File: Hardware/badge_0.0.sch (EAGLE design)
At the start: 43 parts, among them CON1 PH_2, IC1 CP2102, SW1 MK12C02, SW2 MK12C02, U4 MCP73832T-2DCI/OT

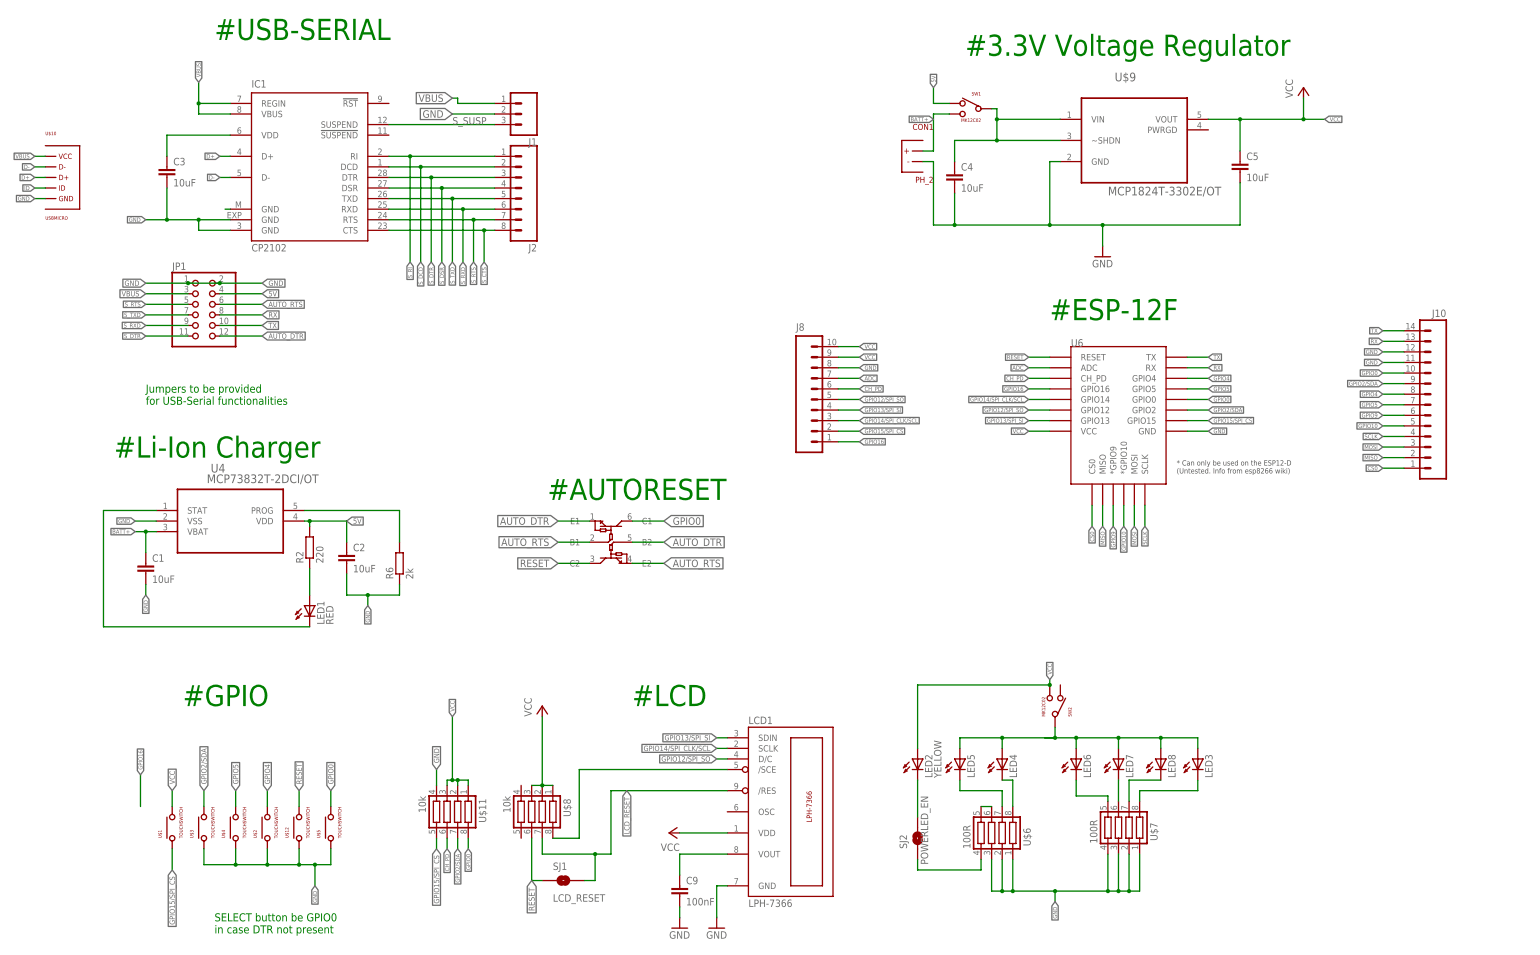
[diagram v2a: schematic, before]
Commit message: Rerouted and labeled some nets
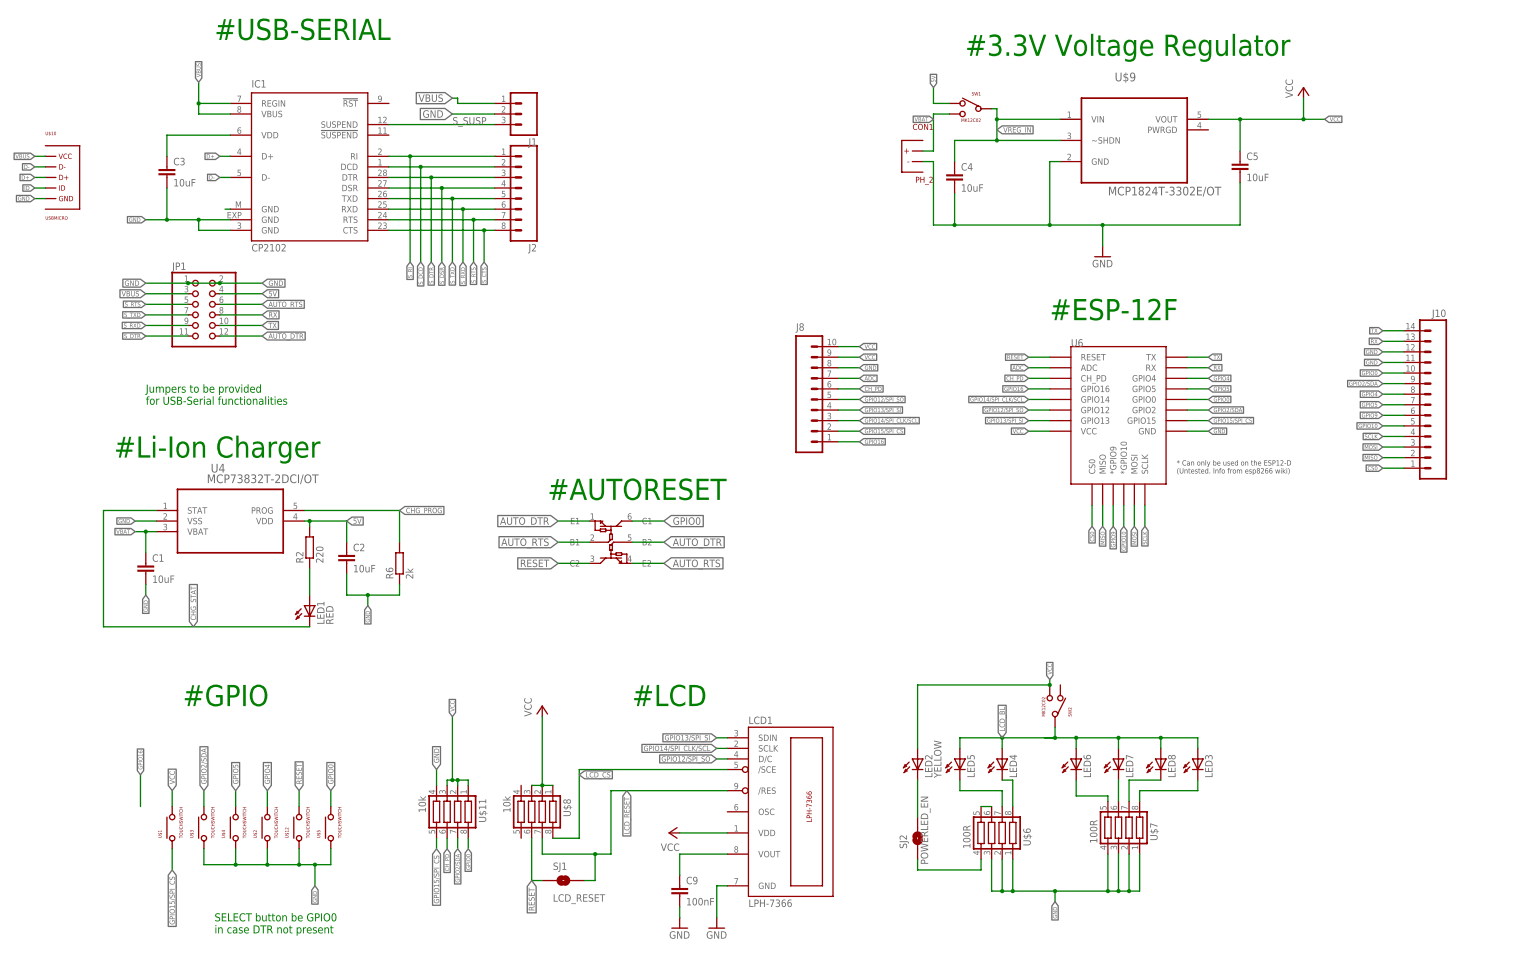
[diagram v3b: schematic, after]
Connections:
- net BATT+ renamed VBAT
- net N$1 renamed VREG_IN
- net N$10 renamed CHG_STAT
- net N$2 renamed LCD_BL
- net N$3 renamed LCD_CS
- net N$6 renamed CHG_PROG
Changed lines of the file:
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@@
 <setting verticaltext="up"/>
 </settings>
-<grid distance="0.05" unitdist="inch" unit="inch" style="lines" multiple="1" display="yes" altdistance="0.01" altunitdist="inch" altunit="inch"/>
+<grid distance="0.05" unitdist="inch" unit="inch" style="lines" multiple="1" display="no" altdistance="0.01" altunitdist="inch" altunit="inch"/>
 <layers>
 <layer number="1" name="Top" color="4" fill="1" visible="no" active="no"/>
@@
 </segment>
 </net>
-<net name="N$3" class="0">
+<net name="LCD_CS" class="0">
 <segment>
 <pinref part="LCD1" gate="G$1" pin="/SCE"/>
@@
 <wire x1="140.97" y1="52.07" x2="147.32" y2="52.07" width="0.1524" layer="91"/>
 <wire x1="147.32" y1="52.07" x2="147.32" y2="68.58" width="0.1524" layer="91"/>
+<label x="147.32" y="67.31" size="1.27" layer="95" xref="yes"/>
 </segment>
 </net>
@@
 </segment>
 </net>
-<net name="N$1" class="0">
+<net name="VREG_IN" class="0">
 <segment>
 <pinref part="SW1" gate="G$1" pin="P$1"/>
@@
 <pinref part="U$9" gate="A" pin="~SHDN"/>
 <wire x1="247.65" y1="219.71" x2="262.89" y2="219.71" width="0.1524" layer="91"/>
+<label x="247.65" y="222.25" size="1.27" layer="95" xref="yes"/>
 </segment>
 </net>
@@
 </segment>
 </net>
-<net name="N$6" class="0">
+<net name="CHG_PROG" class="0">
 <segment>
 <pinref part="U4" gate="A" pin="PROG"/>
@@
 <wire x1="81.28" y1="130.81" x2="104.14" y2="130.81" width="0.1524" layer="91"/>
 <wire x1="104.14" y1="130.81" x2="104.14" y2="123.19" width="0.1524" layer="91"/>
-</segment>
-</net>
-<net name="N$10" class="0">
+<label x="104.14" y="130.81" size="1.27" layer="95" xref="yes"/>
+</segment>
+</net>
+<net name="CHG_STAT" class="0">
 <segment>
 <wire x1="82.55" y1="102.87" x2="33.02" y2="102.87" width="0.1524" layer="91"/>
@@
 <wire x1="33.02" y1="130.81" x2="45.72" y2="130.81" width="0.1524" layer="91"/>
 <pinref part="LED1" gate="G$1" pin="C"/>
-</segment>
-</net>
-<net name="BATT+" class="0">
+<label x="54.61" y="102.87" size="1.27" layer="95" rot="R90" xref="yes"/>
+</segment>
+</net>
+<net name="VBAT" class="0">
 <segment>
 <pinref part="U4" gate="A" pin="VBAT"/>
@@
 </segment>
 </net>
-<net name="N$2" class="0">
+<net name="LCD_BL" class="0">
 <segment>
 <pinref part="LED8" gate="G$1" pin="A"/>
@@
 <junction x="248.92" y="76.2"/>
 <wire x1="238.76" y1="76.2" x2="238.76" y2="73.66" width="0.1524" layer="91"/>
-</segment>
-</net>
+<label x="248.92" y="76.2" size="1.27" layer="95" rot="R90" xref="yes"/>
+</segment>
+</net>

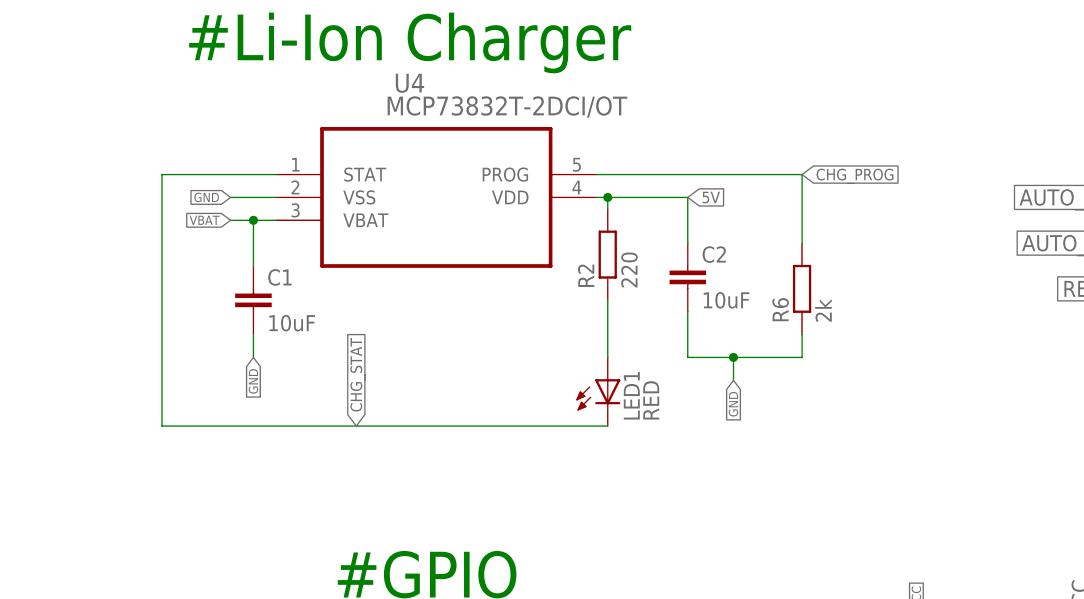
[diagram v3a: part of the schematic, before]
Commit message: Replaced 2 resistors with 1 r-net.
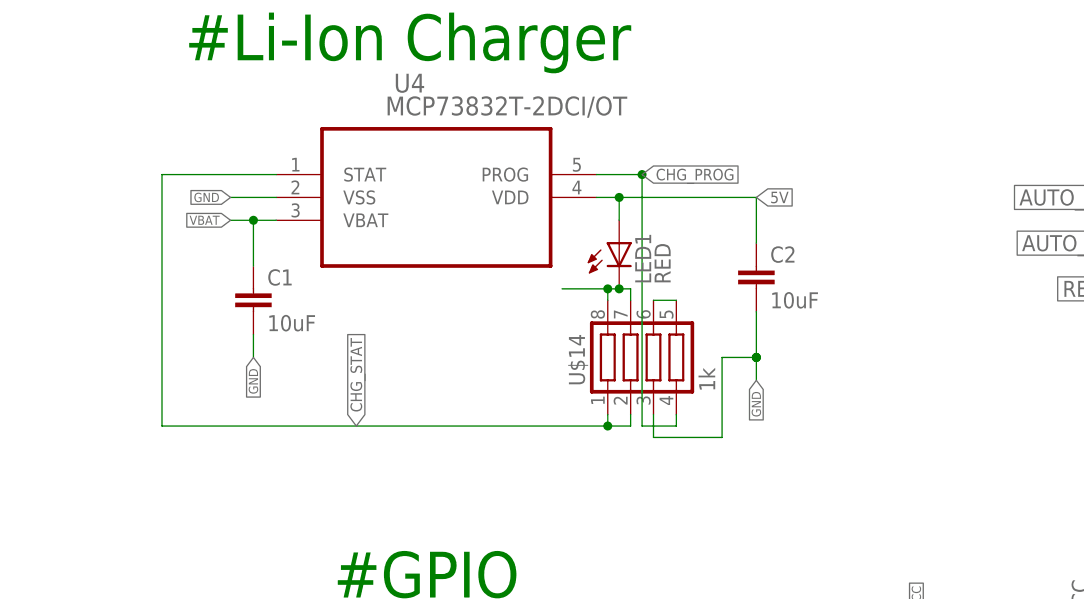
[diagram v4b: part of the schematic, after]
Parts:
- removed R2: 220, resistor:R-EU_R0603W
- removed R6: 2k, resistor:R-EU_R0603W
- added U$14: 1k, Simplex-rlc:RES_ARR
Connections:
- removed net N$4: LED1.A, R2.1
- new net N$1: LED1.C, U$14.7, U$14.8
- new net N$2: U$14.5, U$14.6
- net 5V: now also LED1.A; no longer R2.2
- net CHG_PROG: now also U$14.4; no longer R6.2
- net CHG_STAT: now also U$14.1, U$14.2; no longer LED1.C
- net GND: now also U$14.3; no longer R6.1
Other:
- moved on the sheet: C2, LED1
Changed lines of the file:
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@@
 <part name="LED1" library="led" deviceset="LED" device="SML0805" value="RED"/>
 <part name="LED2" library="led" deviceset="LED" device="SML0805" value="YELLOW"/>
-<part name="R2" library="resistor" deviceset="R-EU_" device="R0603W" value="220"/>
 <part name="C1" library="resistor" deviceset="C-EU" device="C0603K" value="10uF"/>
 <part name="C2" library="resistor" deviceset="C-EU" device="C0603K" value="10uF"/>
-<part name="R6" library="resistor" deviceset="R-EU_" device="R0603W" value="2k"/>
 <part name="J10" library="SparkFun-Connectors" deviceset="M14" device=""/>
 <part name="J8" library="SparkFun-Connectors" deviceset="M10" device="SILK_FEMALE_PTH"/>
@@
 <part name="JP1" library="pinhead" deviceset="PINHD-2X6" device=""/>
 <part name="SJ2" library="SparkFun-Retired" deviceset="SOLDERJUMPER" device="TRACE" value="POWERLED_EN"/>
+<part name="U$14" library="Simplex-rlc" deviceset="RES_ARR" device="" value="1k"/>
 </parts>
 <sheets>
@@
 <instance part="U$9" gate="A" x="280.67" y="222.25"/>
 <instance part="U$10" gate="G$1" x="24.13" y="210.82"/>
-<instance part="LED1" gate="G$1" x="82.55" y="107.95"/>
+<instance part="LED1" gate="G$1" x="83.82" y="123.19"/>
 <instance part="LED2" gate="G$1" x="228.6" y="71.12"/>
-<instance part="R2" gate="G$1" x="82.55" y="121.92" rot="R90"/>
 <instance part="C1" gate="G$1" x="43.18" y="118.11"/>
-<instance part="C2" gate="G$1" x="91.44" y="120.65"/>
-<instance part="R6" gate="G$1" x="104.14" y="118.11" rot="R90"/>
+<instance part="C2" gate="G$1" x="99.06" y="120.65"/>
 <instance part="J10" gate="G$1" x="355.6" y="158.75" rot="MR0"/>
 <instance part="J8" gate="G$1" x="199.39" y="165.1"/>
@@
 <attribute name="VALUE" x="231.14" y="45.72" size="1.778" layer="96" rot="R90"/>
 </instance>
+<instance part="U$14" gate="G$1" x="85.09" y="109.22" rot="R90"/>
 </instances>
 <busses>
@@
 </segment>
 <segment>
-<pinref part="R6" gate="G$1" pin="1"/>
-<wire x1="104.14" y1="113.03" x2="104.14" y2="110.49" width="0.1524" layer="91"/>
-<wire x1="96.52" y1="110.49" x2="104.14" y2="110.49" width="0.1524" layer="91"/>
-<wire x1="96.52" y1="110.49" x2="96.52" y2="107.95" width="0.1524" layer="91"/>
-<label x="96.52" y="107.95" size="1.016" layer="95" rot="R270" xref="yes"/>
+<wire x1="99.06" y1="110.49" x2="99.06" y2="107.95" width="0.1524" layer="91"/>
+<label x="99.06" y="107.95" size="1.016" layer="95" rot="R270" xref="yes"/>
 <pinref part="C2" gate="G$1" pin="2"/>
-<wire x1="91.44" y1="115.57" x2="91.44" y2="110.49" width="0.1524" layer="91"/>
-<wire x1="91.44" y1="110.49" x2="96.52" y2="110.49" width="0.1524" layer="91"/>
-<junction x="96.52" y="110.49"/>
+<wire x1="99.06" y1="115.57" x2="99.06" y2="110.49" width="0.1524" layer="91"/>
+<junction x="99.06" y="110.49"/>
+<wire x1="95.25" y1="110.49" x2="99.06" y2="110.49" width="0.1524" layer="91"/>
+<junction x="99.06" y="110.49"/>
+<wire x1="95.25" y1="101.6" x2="95.25" y2="110.49" width="0.1524" layer="91"/>
+<pinref part="U$14" gate="G$1" pin="3"/>
+<wire x1="87.63" y1="104.14" x2="87.63" y2="101.6" width="0.1524" layer="91"/>
+<wire x1="87.63" y1="101.6" x2="95.25" y2="101.6" width="0.1524" layer="91"/>
 </segment>
 <segment>
@@
 <segment>
 <pinref part="U4" gate="A" pin="PROG"/>
-<pinref part="R6" gate="G$1" pin="2"/>
-<wire x1="81.28" y1="130.81" x2="104.14" y2="130.81" width="0.1524" layer="91"/>
-<wire x1="104.14" y1="130.81" x2="104.14" y2="123.19" width="0.1524" layer="91"/>
-<label x="104.14" y="130.81" size="1.27" layer="95" xref="yes"/>
+<wire x1="81.28" y1="130.81" x2="86.36" y2="130.81" width="0.1524" layer="91"/>
+<label x="86.36" y="130.81" size="1.27" layer="95" xref="yes"/>
+<wire x1="86.36" y1="102.87" x2="86.36" y2="130.81" width="0.1524" layer="91"/>
+<junction x="86.36" y="130.81"/>
+<pinref part="U$14" gate="G$1" pin="4"/>
+<wire x1="86.36" y1="102.87" x2="90.17" y2="102.87" width="0.1524" layer="91"/>
+<wire x1="90.17" y1="102.87" x2="90.17" y2="104.14" width="0.1524" layer="91"/>
 </segment>
 </net>
 <net name="CHG_STAT" class="0">
 <segment>
-<wire x1="82.55" y1="102.87" x2="33.02" y2="102.87" width="0.1524" layer="91"/>
 <wire x1="33.02" y1="102.87" x2="33.02" y2="130.81" width="0.1524" layer="91"/>
 <pinref part="U4" gate="A" pin="STAT"/>
 <wire x1="33.02" y1="130.81" x2="45.72" y2="130.81" width="0.1524" layer="91"/>
-<pinref part="LED1" gate="G$1" pin="C"/>
 <label x="54.61" y="102.87" size="1.27" layer="95" rot="R90" xref="yes"/>
+<wire x1="33.02" y1="102.87" x2="82.55" y2="102.87" width="0.1524" layer="91"/>
+<pinref part="U$14" gate="G$1" pin="1"/>
+<wire x1="82.55" y1="102.87" x2="85.09" y2="102.87" width="0.1524" layer="91"/>
+<wire x1="82.55" y1="104.14" x2="82.55" y2="102.87" width="0.1524" layer="91"/>
+<junction x="82.55" y="102.87"/>
+<pinref part="U$14" gate="G$1" pin="2"/>
+<wire x1="85.09" y1="104.14" x2="85.09" y2="102.87" width="0.1524" layer="91"/>
 </segment>
 </net>
@@
 </segment>
 </net>
-<net name="N$4" class="0">
-<segment>
-<pinref part="LED1" gate="G$1" pin="A"/>
-<pinref part="R2" gate="G$1" pin="1"/>
-<wire x1="82.55" y1="110.49" x2="82.55" y2="116.84" width="0.1524" layer="91"/>
-</segment>
-</net>
 <net name="N$9" class="0">
 <segment>
@@
 <pinref part="U4" gate="A" pin="VDD"/>
 <pinref part="C2" gate="G$1" pin="1"/>
-<wire x1="81.28" y1="128.27" x2="82.55" y2="128.27" width="0.1524" layer="91"/>
-<wire x1="82.55" y1="128.27" x2="91.44" y2="128.27" width="0.1524" layer="91"/>
-<wire x1="91.44" y1="128.27" x2="91.44" y2="123.19" width="0.1524" layer="91"/>
-<pinref part="R2" gate="G$1" pin="2"/>
-<wire x1="82.55" y1="127" x2="82.55" y2="128.27" width="0.1524" layer="91"/>
-<junction x="82.55" y="128.27"/>
-<label x="91.44" y="128.27" size="1.27" layer="95" xref="yes"/>
+<wire x1="81.28" y1="128.27" x2="83.82" y2="128.27" width="0.1524" layer="91"/>
+<wire x1="83.82" y1="128.27" x2="99.06" y2="128.27" width="0.1524" layer="91"/>
+<wire x1="99.06" y1="128.27" x2="99.06" y2="123.19" width="0.1524" layer="91"/>
+<label x="99.06" y="128.27" size="1.27" layer="95" xref="yes"/>
+<pinref part="LED1" gate="G$1" pin="A"/>
+<wire x1="83.82" y1="128.27" x2="83.82" y2="125.73" width="0.1524" layer="91"/>
+<junction x="83.82" y="128.27"/>
 </segment>
 </net>
@@
 </segment>
 </net>
+<net name="N$1" class="0">
+<segment>
+<pinref part="LED1" gate="G$1" pin="C"/>
+<wire x1="83.82" y1="118.11" x2="82.55" y2="118.11" width="0.1524" layer="91"/>
+<pinref part="U$14" gate="G$1" pin="8"/>
+<wire x1="82.55" y1="118.11" x2="77.47" y2="118.11" width="0.1524" layer="91"/>
+<wire x1="82.55" y1="118.11" x2="82.55" y2="116.84" width="0.1524" layer="91"/>
+<junction x="82.55" y="118.11"/>
+<pinref part="U$14" gate="G$1" pin="7"/>
+<wire x1="83.82" y1="118.11" x2="85.09" y2="118.11" width="0.1524" layer="91"/>
+<wire x1="85.09" y1="118.11" x2="85.09" y2="116.84" width="0.1524" layer="91"/>
+<junction x="83.82" y="118.11"/>
+</segment>
+</net>
+<net name="N$2" class="0">
+<segment>
+<pinref part="U$14" gate="G$1" pin="6"/>
+<pinref part="U$14" gate="G$1" pin="5"/>
+<wire x1="87.63" y1="116.84" x2="90.17" y2="116.84" width="0.1524" layer="91"/>
+</segment>
+</net>

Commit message: Added IO16 <-> Reset; Added mounting holes for LCD; Removed notice for Cutout
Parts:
- added JP2: (no value), SparkFun-Retired:JUMPER-2SMD-NO
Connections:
- net GPIO16: now also JP2.2
- net RESET: now also JP2.1
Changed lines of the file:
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@@
 <?xml version="1.0" encoding="utf-8"?>
 <!DOCTYPE eagle SYSTEM "eagle.dtd">
-<eagle version="7.1.0">
+<eagle version="7.5.0">
 <drawing>
 <settings>
@@
 <setting verticaltext="up"/>
 </settings>
-<grid distance="0.05" unitdist="inch" unit="inch" style="lines" multiple="1" display="no" altdistance="0.01" altunitdist="inch" altunit="inch"/>
+<grid distance="0.1" unitdist="inch" unit="inch" style="lines" multiple="1" display="no" altdistance="0.01" altunitdist="inch" altunit="inch"/>
 <layers>
 <layer number="1" name="Top" color="4" fill="1" visible="no" active="no"/>
@@
 <part name="SJ2" library="SparkFun-Retired" deviceset="SOLDERJUMPER" device="TRACE" value="POWERLED_EN"/>
 <part name="U$14" library="Simplex-rlc" deviceset="RES_ARR" device="" value="1k"/>
+<part name="JP2" library="SparkFun-Retired" deviceset="JUMPER-2" device="SMD-NO"/>
 </parts>
 <sheets>
@@
 </instance>
 <instance part="U$14" gate="G$1" x="85.09" y="109.22" rot="R90"/>
+<instance part="JP2" gate="A" x="38.1" y="53.34" rot="R90"/>
 </instances>
 <busses>
@@
 <label x="135.89" y="41.91" size="1.4224" layer="95" rot="R270" xref="yes"/>
 </segment>
+<segment>
+<wire x1="41.91" y1="53.34" x2="41.91" y2="44.45" width="0.1524" layer="91"/>
+<pinref part="JP2" gate="A" pin="1"/>
+<wire x1="40.64" y1="53.34" x2="41.91" y2="53.34" width="0.1524" layer="91"/>
+<label x="41.91" y="44.45" size="1.016" layer="95" rot="R270" xref="yes"/>
+</segment>
 </net>
 <net name="ADC" class="0">
@@
 </segment>
 <segment>
-<wire x1="41.91" y1="67.31" x2="41.91" y2="59.69" width="0.1524" layer="91"/>
+<wire x1="41.91" y1="67.31" x2="41.91" y2="55.88" width="0.1524" layer="91"/>
 <label x="41.91" y="67.31" size="1.016" layer="95" rot="R90" xref="yes"/>
-</segment>
-</net>
+<pinref part="JP2" gate="A" pin="2"/>
+<wire x1="40.64" y1="55.88" x2="41.91" y2="55.88" width="0.1524" layer="91"/>
+</segment>
+</net>

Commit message: before teardown
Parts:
- added J3: (no value), SparkFun-Connectors:M12PTH
- added J4: (no value), SparkFun-Connectors:M08
- added J5: (no value), SparkFun-Connectors:M05PTH
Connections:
- net ADC: now also J3.2
- net CH_PD: now also J3.3
- net CS0: now also J3.12
- net GPIO0: now also J4.3
- net GPIO10: now also J4.8
- net GPIO12/SPI_SO: now also J3.4
- net GPIO13/SPI_SI: now also J3.5
- net GPIO14/SPI_CLK/SCL: now also J3.6
- net GPIO15/SPI_CS: now also J3.7
- net GPIO16: now also J3.8
- net GPIO2/SDA: now also J4.4
- net GPIO4: now also J4.5
- net GPIO5: now also J4.6
- net GPIO9: now also J4.7
- net MISO: now also J3.11
- net MOSI: now also J3.10
- net RESET: now also J3.1
- net RX: now also J4.2
- net SCLK: now also J3.9
- net TX: now also J4.1
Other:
- moved on the sheet: J10, J8
